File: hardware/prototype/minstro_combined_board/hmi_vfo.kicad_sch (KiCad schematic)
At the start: 1 part

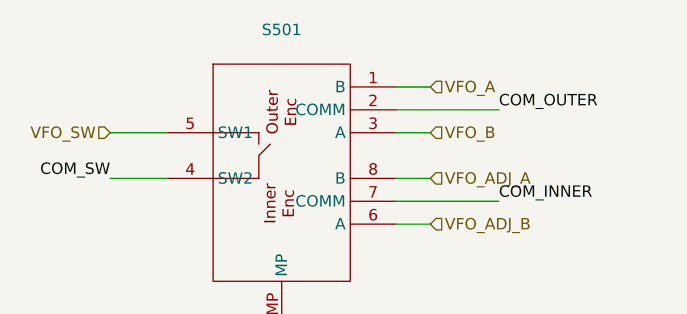
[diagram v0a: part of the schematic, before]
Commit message: Combined board started layout
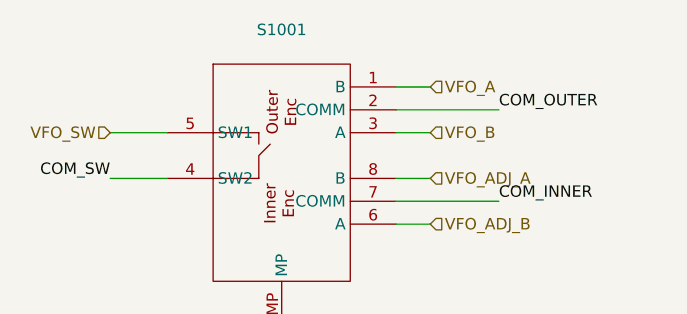
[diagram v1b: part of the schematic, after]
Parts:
- renumbered S501 to S1001
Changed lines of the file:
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@@
 		(dnp no)
 		(fields_autoplaced yes)
-		(property "Reference" "S501"
+		(property "Reference" "S1001"
 			(at 127 73.66 0)
 			(effects
@@
 			(project ""
 				(path "/edc2d64f-9cdb-4ab0-b2de-c3cfa55e1c10/0056968a-0c1d-4a8a-9224-b2ac4a6e25ff"
-					(reference "S501")
+					(reference "S1001")
 					(unit 1)
 				)
@@
 		(dnp no)
 		(fields_autoplaced yes)
-		(property "Reference" "#PWR0501"
+		(property "Reference" "#PWR01001"
 			(at 176.53 91.44 0)
 			(effects
@@
 			(project ""
 				(path "/edc2d64f-9cdb-4ab0-b2de-c3cfa55e1c10/0056968a-0c1d-4a8a-9224-b2ac4a6e25ff"
-					(reference "#PWR0501")
+					(reference "#PWR01001")
 					(unit 1)
 				)

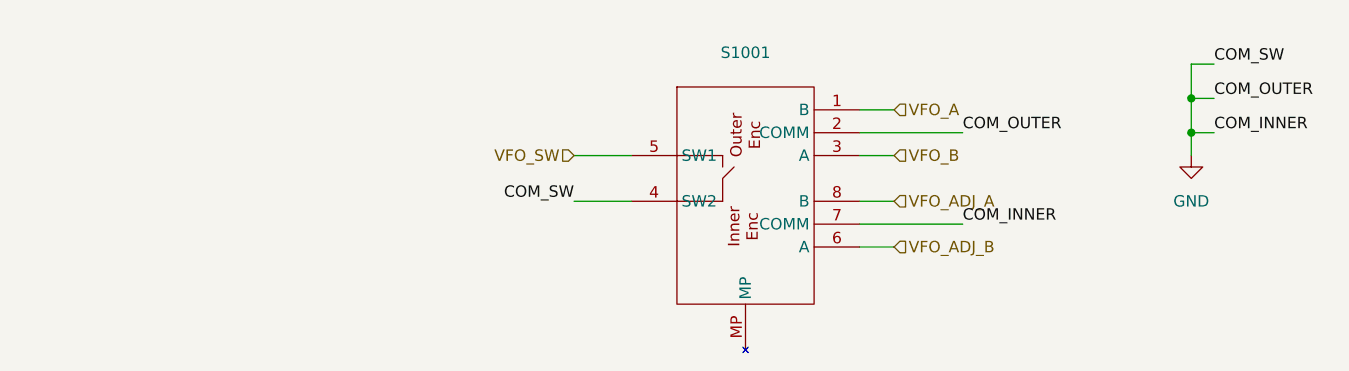
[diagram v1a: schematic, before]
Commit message: Schematic ERC complete
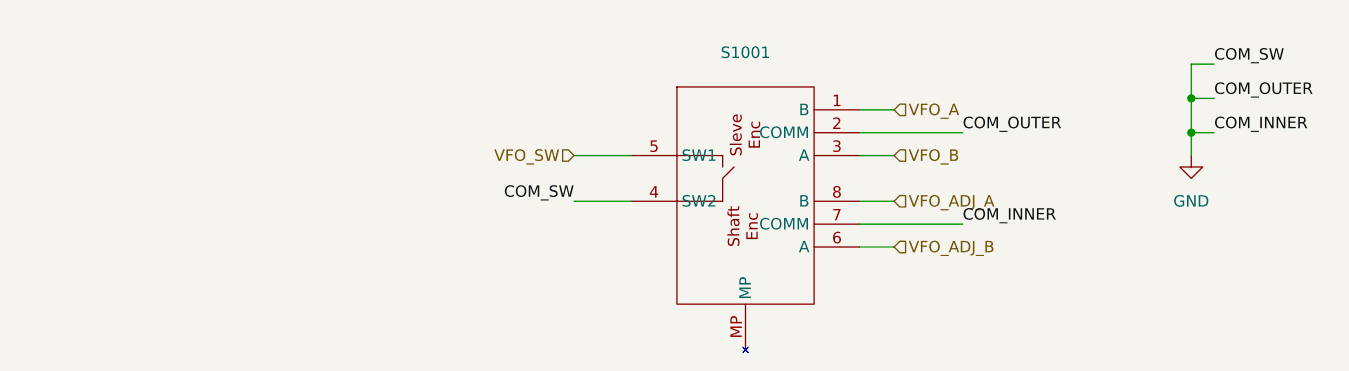
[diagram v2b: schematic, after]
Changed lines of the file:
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@@
-		(pin "5"
-		)
 		(pin "5"
 		)
@@
 				)
 			)
-			(project ""
+			(project "minstro_combined_board"
 				(path "/edc2d64f-9cdb-4ab0-b2de-c3cfa55e1c10/0056968a-0c1d-4a8a-9224-b2ac4a6e25ff"
 					(reference "S1001")
@@
 				)
 			)
-			(project ""
+			(project "minstro_combined_board"
 				(path "/edc2d64f-9cdb-4ab0-b2de-c3cfa55e1c10/0056968a-0c1d-4a8a-9224-b2ac4a6e25ff"
 					(reference "#PWR01001")

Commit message: Layout WIP
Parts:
- added J1001: VFO, Connector_PinHeader_2.54mm:PinHeader_1x06_P2.54mm_Vertical, symbol Connector_Generic:Conn_01x06
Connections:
- net GND: now also J1001.1 (Pin_1)
- net VFO_A: now also J1001.2 (Pin_2)
- net VFO_ADJ_A: now also J1001.4 (Pin_4)
- net VFO_ADJ_B: now also J1001.5 (Pin_5)
- net VFO_B: now also J1001.3 (Pin_3)
- net VFO_SW: now also J1001.6 (Pin_6)

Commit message: Layout WIP
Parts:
- J1001: footprint Connector_PinHeader_2.54mm:PinHeader_1x06_P2.54mm_Vertical -> BVH_PinHeader_FrictionRetention:PinHeader_1x06_P2.54mm_Vertical
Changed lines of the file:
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@@
 			)
 		)
-		(property "Footprint" "Connector_PinHeader_2.54mm:PinHeader_1x06_P2.54mm_Vertical"
+		(property "Footprint" "BVH_PinHeader_FrictionRetention:PinHeader_1x06_P2.54mm_Vertical"
 			(at 49.53 82.55 0)
 			(effects

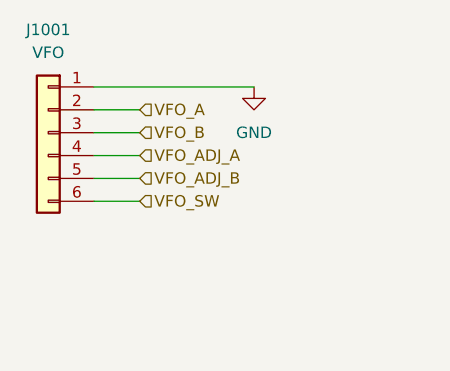
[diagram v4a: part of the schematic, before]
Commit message: PCB size fix started
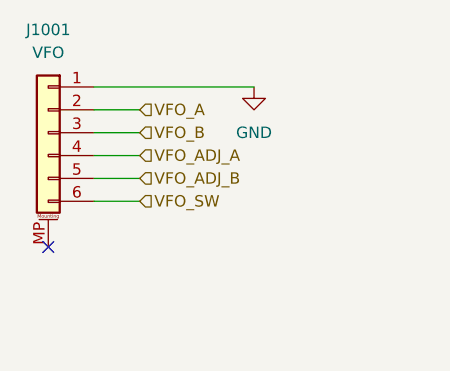
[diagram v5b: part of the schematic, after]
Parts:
- J1001: footprint BVH_PinHeader_FrictionRetention:PinHeader_1x06_P2.54mm_Vertical -> BVH_Connectors_Misc:Anchored_PinHeader_1x06_P2.54mm_Vertical_M2.5; symbol Connector_Generic:Conn_01x06 -> Connector_Generic_MountingPin:Conn_01x06_MountingPin
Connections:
- no-connect marks 0 -> 1
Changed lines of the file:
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@@
 		(color 0 0 0 0)
+	)
+	(no_connect
+		(at 49.53 95.25)
 	)
 	(wire
@@
 	)
 	(symbol
-		(lib_id "Connector_Generic:Conn_01x06")
+		(lib_id "Connector_Generic_MountingPin:Conn_01x06_MountingPin")
 		(at 49.53 82.55 0)
 		(mirror y)
@@
 			)
 		)
-		(property "Footprint" "BVH_PinHeader_FrictionRetention:PinHeader_1x06_P2.54mm_Vertical"
+		(property "Footprint" "BVH_Connectors_Misc:Anchored_PinHeader_1x06_P2.54mm_Vertical_M2.5"
 			(at 49.53 82.55 0)
 			(effects
@@
 			)
 		)
-		(property "Description" "Generic connector, single row, 01x06, script generated (kicad-library-utils/schlib/autogen/connector/)"
+		(property "Description" "Generic connectable mounting pin connector, single row, 01x06, script generated (kicad-library-utils/schlib/autogen/connector/)"
 			(at 49.53 82.55 0)
 			(effects
@@
 		(pin "6"
 		)
+		(pin "MP"
+		)
 		(instances

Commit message: Layout completed, initial review
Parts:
- removed S1001: ~, BVH_Switches:Alps_EC11E_Dual_Shaft_Rotary_Encoder_With_Switch, symbol BVH_Switches_Inputs:Rotary_Encoder_Dual_Axis_Switch
- J1001: footprint BVH_Connectors_Misc:Anchored_PinHeader_1x06_P2.54mm_Vertical_M2.5 -> BVH_PinHeader_FrictionRetention:PinHeader_1x06_P2.54mm_Vertical; symbol Connector_Generic_MountingPin:Conn_01x06_MountingPin -> Connector_Generic:Conn_01x06
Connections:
- no-connect marks 1 -> 0
